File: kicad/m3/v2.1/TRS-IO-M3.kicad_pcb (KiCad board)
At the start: 2 copper layers, 134 x 74.2 mm, 45 parts, among them J1 Conn_02x25_Odd_Even, J2 Conn_02x25_Odd_Even, J3 Conn_01x19, J4 Conn_01x02_Male, J5 Conn_01x06_Male, J6 Conn_01x06_Male, J7 AudioJack3, Q1 2N7002, Q2 2N7002, Q3 2N7002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

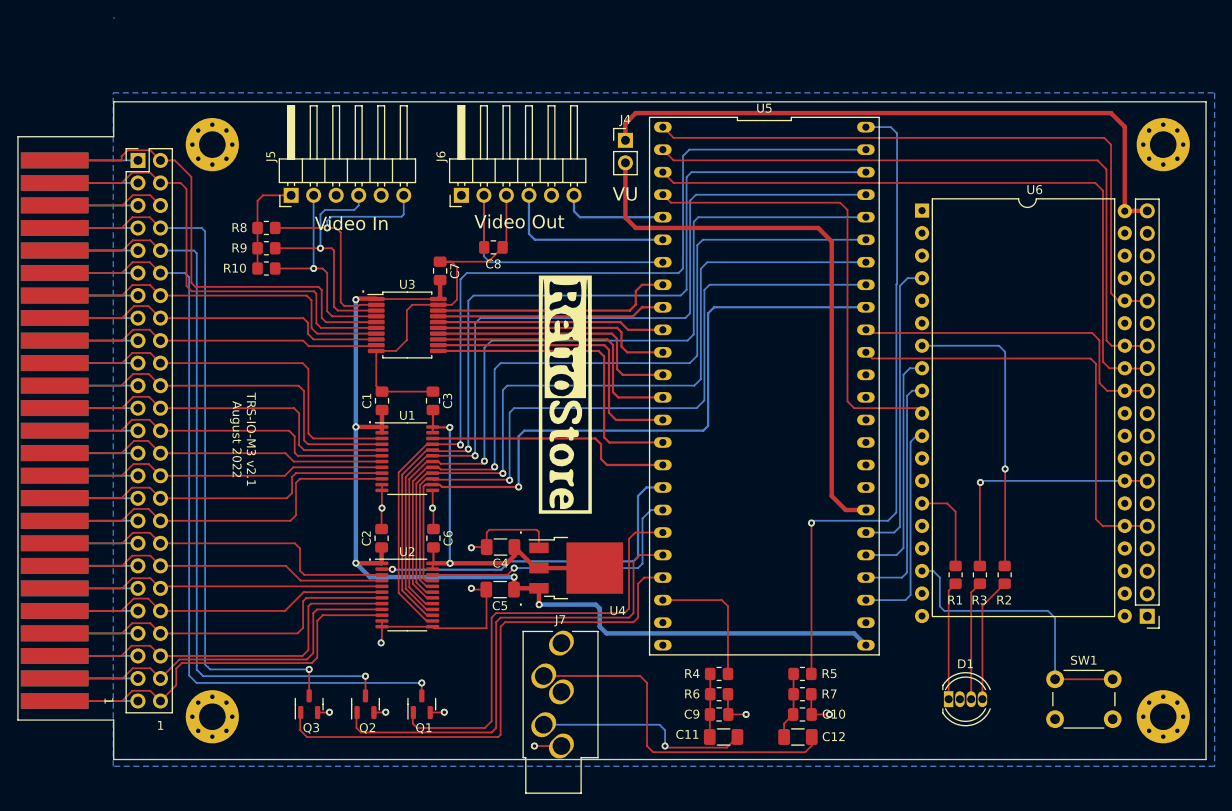
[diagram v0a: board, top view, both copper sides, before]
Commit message: TRS-IO-M3 silkscreen fixes
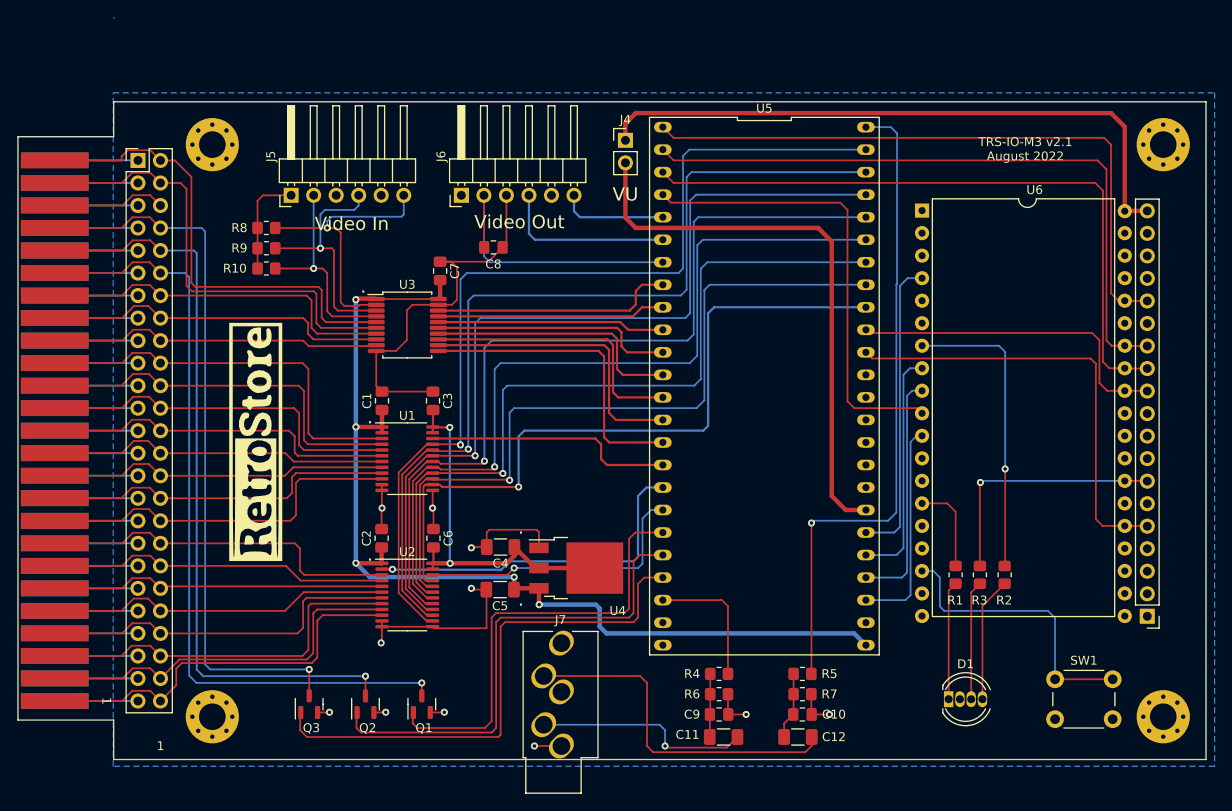
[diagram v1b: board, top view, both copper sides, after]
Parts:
- moved G1 35.5 mm to (129.5, 94.5), turned to 90 degrees
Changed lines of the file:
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@@
   )
   (footprint "LOGO" (layer "F.Cu")
-    (at 164.592 89.154 -90)
+    (at 129.54 94.488 90)
     (attr board_only exclude_from_pos_files exclude_from_bom)
     (fp_text reference "G1" (at 0 0 90) (layer "F.SilkS") hide
@@
   (gr_line (start 102.7938 125.857) (end 113.5888 125.857) (layer "Edge.Cuts") (width 0.05))
   (gr_line (start 102.7938 60.071) (end 113.5888 60.071) (layer "Edge.Cuts") (width 0.05))
-  (gr_text "1" (at 113.03 123.698 270) (layer "F.SilkS")
+  (gr_text "1" (at 112.776 123.698 270) (layer "F.SilkS")
     (effects (font (size 1 1) (thickness 0.15)))
   )
@@
     (effects (font (size 1.5 1.5) (thickness 0.3)))
   )
-  (gr_text "TRS-IO-M3 v2.1\nAugust 2022" (at 128.27 94.234 270) (layer "F.SilkS")
+  (gr_text "TRS-IO-M3 v2.1\nAugust 2022" (at 216.408 61.468) (layer "F.SilkS")
     (effects (font (size 1 1) (thickness 0.15)))
   )
@@
     (effects (font (size 1.5 1.5) (thickness 0.3)))
   )
-  (gr_text "1" (at 118.872 126.492) (layer "F.SilkS")
+  (gr_text "1" (at 118.872 128.778) (layer "F.SilkS")
     (effects (font (size 1 1) (thickness 0.15)))
   )
